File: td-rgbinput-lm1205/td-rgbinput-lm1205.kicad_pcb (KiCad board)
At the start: 2 copper layers, 100 x 50 mm, 59 parts, among them J1 Conn_01x10_Socket, J16 Conn_01x06_Male, J17 Conn_01x06_Male, J2 Conn_01x07_Male, J3 Conn_01x05_Pin, J4 Conn_01x06_Male, J5 DB15_Female_HighDensity, U1 AP2204K-3.3, U11 24LC08, U18 LM1205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

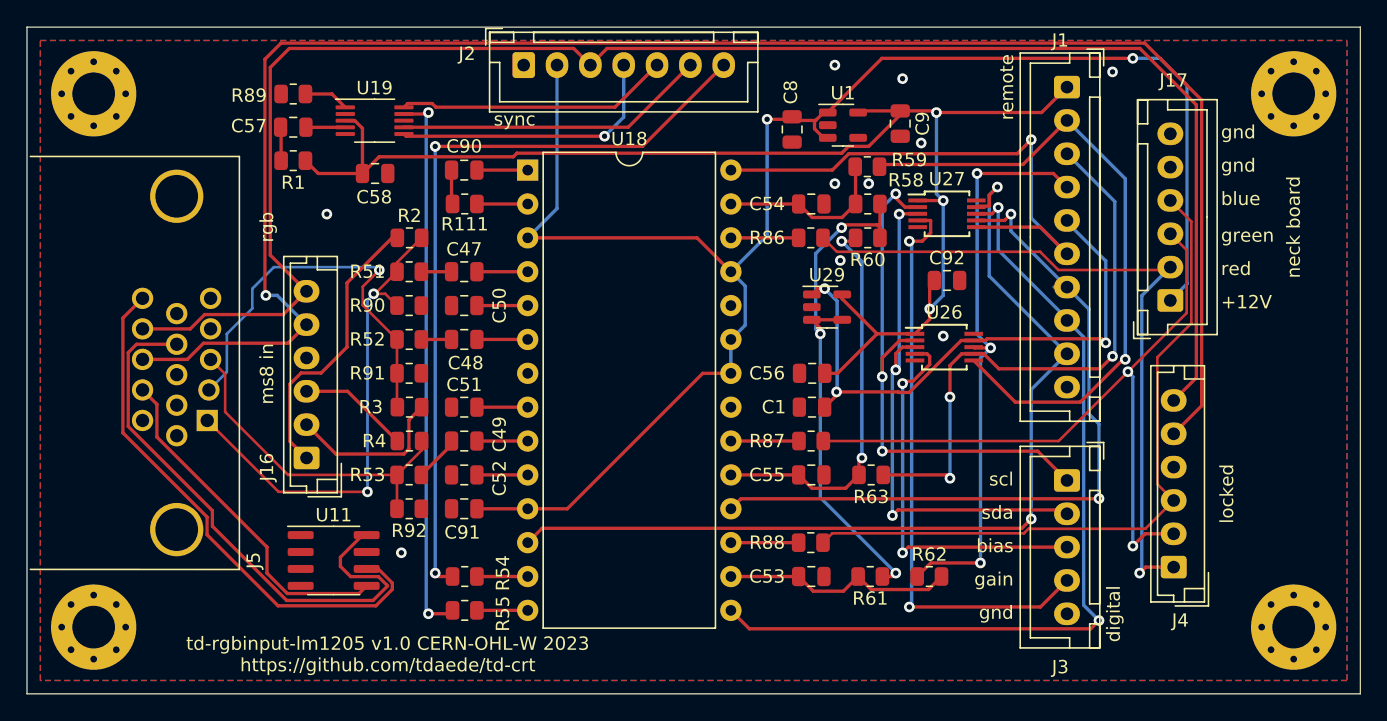
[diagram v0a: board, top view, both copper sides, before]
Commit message: Update td-rgbinput-lm1205 to add decoupling caps etc
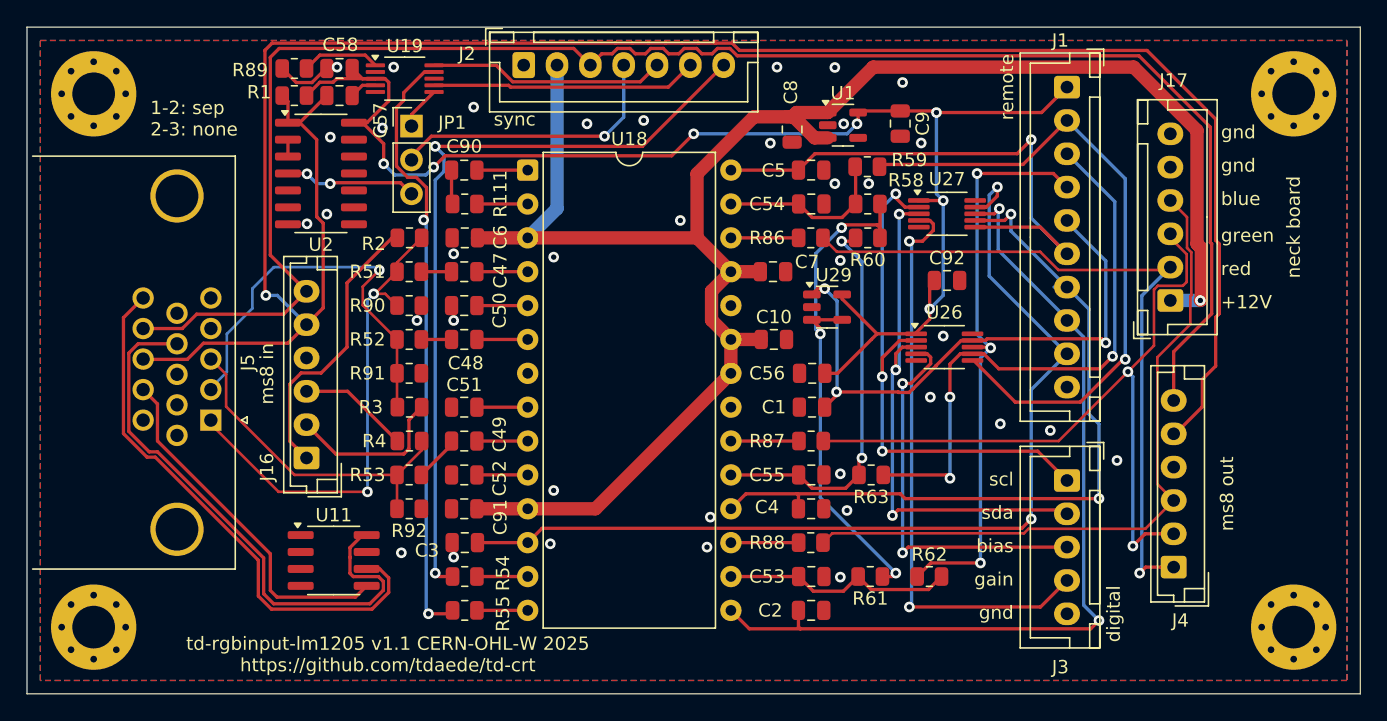
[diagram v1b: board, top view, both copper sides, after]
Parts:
- added C10: 1uF, Capacitor_SMD:C_0805_2012Metric, F.Cu at (128.0, 74.4)
- added C2: 0.1uF, Capacitor_SMD:C_0805_2012Metric, F.Cu at (130.8, 94.7)
- added C3: 0.1uF, Capacitor_SMD:C_0805_2012Metric, F.Cu at (104.8, 89.7)
- added C4: 0.1uF, Capacitor_SMD:C_0805_2012Metric, F.Cu at (130.8, 87.1)
- added C5: 0.1uF, Capacitor_SMD:C_0805_2012Metric, F.Cu at (130.8, 61.7)
- added C6: 1uF, Capacitor_SMD:C_0805_2012Metric, F.Cu at (104.8, 66.8)
- added C7: 1uF, Capacitor_SMD:C_0805_2012Metric, F.Cu at (128.0, 69.3)
- added JP1: Jumper_3_Bridged12, Connector_PinHeader_2.54mm:PinHeader_1x03_P2.54mm_Vertical, F.Cu at (100.8, 58.4)
- added U2: 74HCT14, Package_SO:SOIC-14_3.9x8.7mm_P1.27mm, F.Cu at (94.0, 62.0)
- C91: value 0.1uF -> 1uF
- J5: footprint td-io:DSUB-15-HD_Female_Horizontal_P2.29x2.5mm_EdgePinOffset8.35mm_Housed_MountingHolesOffset10.89mm -> Connector_Dsub:DSUB-15-HD_Socket_Horizontal_P2.29x2.54mm_EdgePinOffset8.35mm_Housed_MountingHolesOffset10.89mm
- U1: value AP2204K-3.3 -> AP2205-33W5-7
- moved C58 8.32 mm to (95.4, 54.1), turned to 180 degrees
- moved R1 4.88 mm to (92.1, 56.1)
- moved C57 4.20 mm to (95.4, 56.1)
- moved U19 3.88 mm to (100.3, 54.9)
- moved R89 1.92 mm to (92.1, 54.1)
- moved J5 1.29 mm to (85.8, 80.5)
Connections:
- C57 pad 2: /rgb/hsync_vga -> vga_hsync
- J2 pad 4: SEP_HSYNC -> Net-(J2-Pin_4)
- J5 pad 0: (no net) -> GND
- R1 pad 2: /rgb/hsync_vga -> vga_hsync
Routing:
- net vga_hsync: track 133.5 -> 157.2 mm
- net Net-(J2-Pin_4): track 0.00 -> 21.3 mm, vias 0 -> 1
- net SEP_HSYNC: track 21.0 -> 3.26 mm, vias 1 -> 0
- net PLAIN_HSYNC: track 0.00 -> 9.96 mm, vias 0 -> 2
- net +12V: track 127.5 -> 136.8 mm, vias 2 -> 1
- net SEP_BP: track 41.5 -> 46.1 mm
- net GND: track 0.00 -> 4.22 mm, vias 10 -> 37
- net +3.3V: track 102.5 -> 106.7 mm, vias 3 -> 7
- net /rgb/globalgain: track 69.9 -> 73.6 mm
- net SEP_VSYNC: track 23.4 -> 20.0 mm
- net SEP_OE: track 20.5 -> 17.8 mm
- net /rgb/hsync_vga: track 2.53 -> 0.00 mm
- net Net-(U19-Rext): track 3.40 -> 5.90 mm
- net vga_vsync: track 127.1 -> 129.1 mm
- net /rgb/ggain: track 55.8 -> 57.2 mm
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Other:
- board text added: "1-2: sep 2-3: none"
- board text added: "ms8 out"
- board text added: "td-rgbinput-lm1205 v1.1 CERN-OHL-W 2025 https://github.com/tdaede/td-crt"
- board text removed: "locked"
- board text removed: "rgb"
- board text removed: "td-rgbinput-lm1205 v1.0 CERN-OHL-W 2023 https://github.com/tdaede/td-crt"
